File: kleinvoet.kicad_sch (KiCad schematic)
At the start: 33 parts, among them SW101 RESET, SW102 USER, U101 STM32F446RETx, Y101 12 MHz, Y102 32.768 kHz

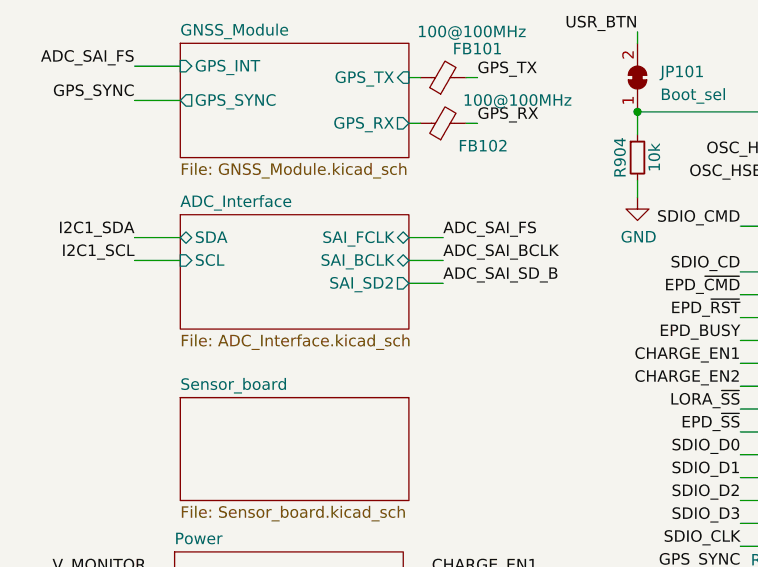
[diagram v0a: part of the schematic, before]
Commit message: (sch) fix SAI pinout
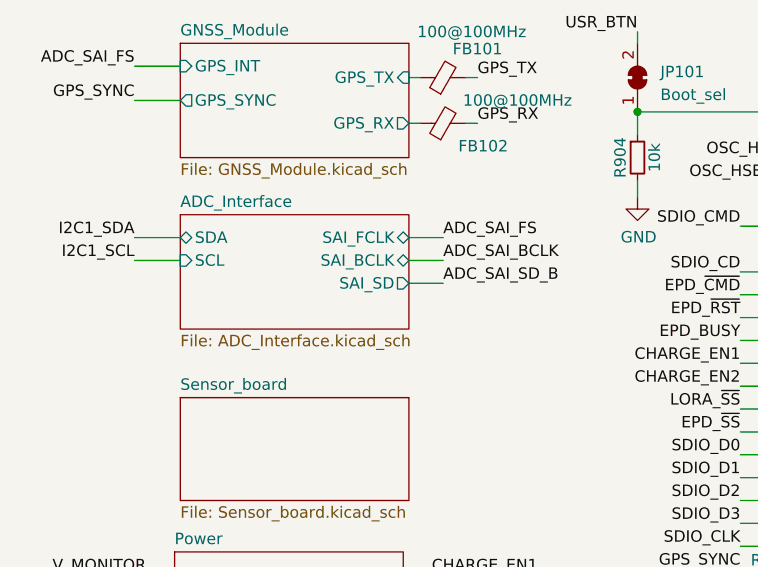
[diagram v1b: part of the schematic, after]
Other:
- sheet ADC_Interface ports: added SAI_SD; removed SAI_SD2
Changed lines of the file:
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@@
       (effects (font (size 1.27 1.27)) (justify left top))
     )
-    (pin "SAI_SD2" output (at 57.15 60.96 0)
+    (pin "SAI_SD" output (at 57.15 60.96 0)
       (effects (font (size 1.27 1.27)) (justify right))
     )

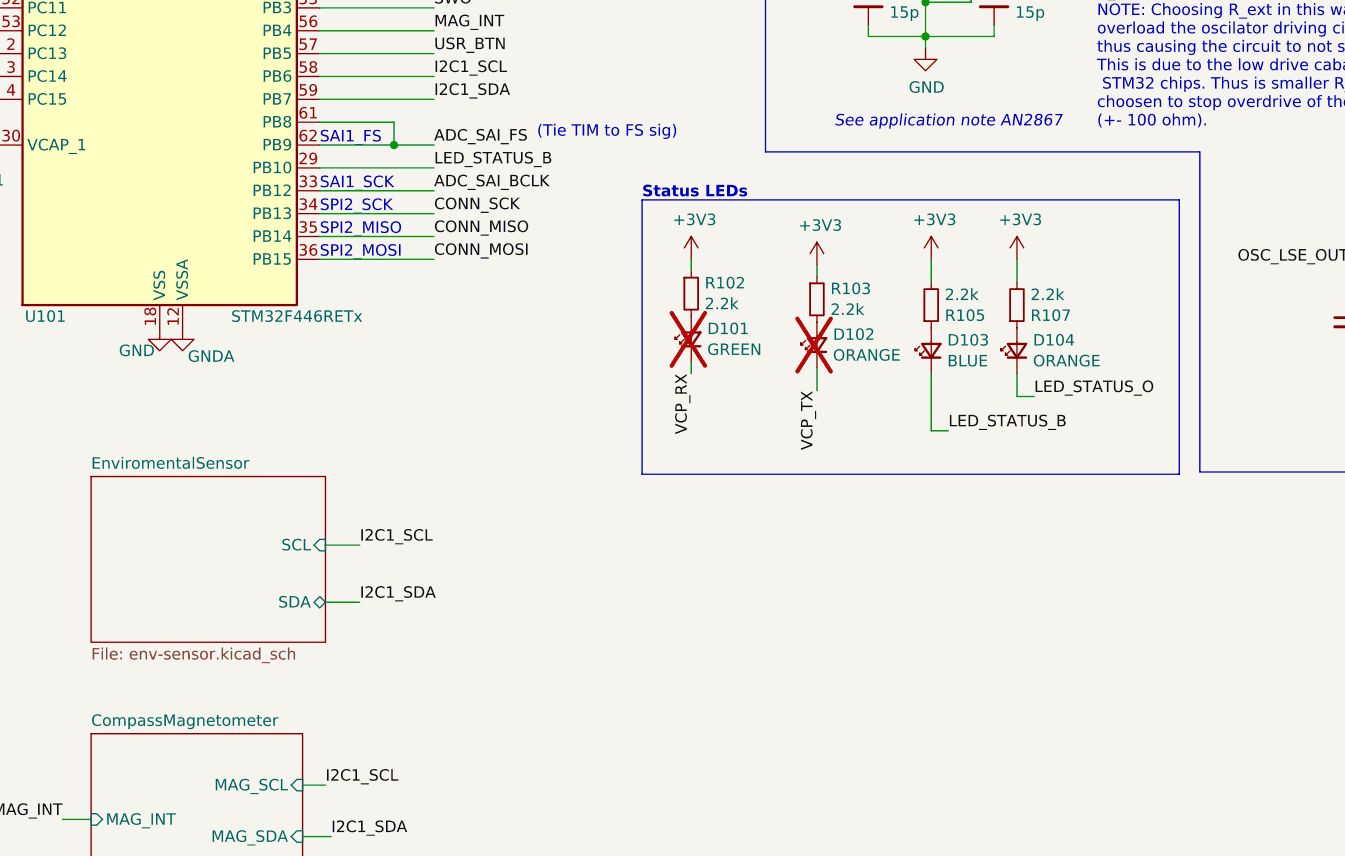
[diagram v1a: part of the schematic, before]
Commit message: (sch) add neopixel placeholder
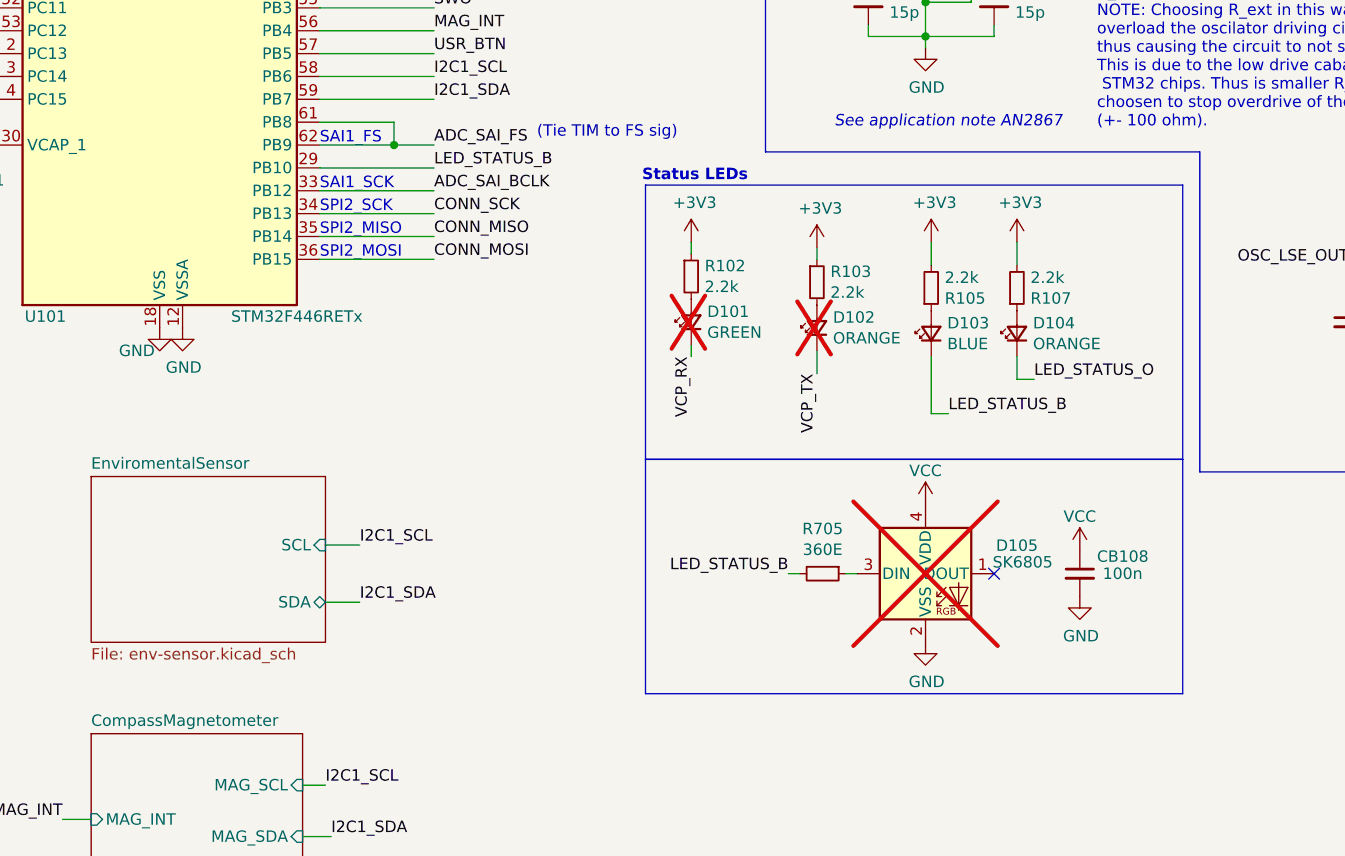
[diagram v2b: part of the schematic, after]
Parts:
- added CB108: 100n, Capacitor_SMD:C_0402_1005Metric, symbol Device:C_Small
- added D105: SK6805, grootvoet:LED_SK6805_PLCC4_2.4x2.7mm_P1.3mm, symbol LED:SK6805
- added R705: 360E, Resistor_SMD:R_0402_1005Metric, symbol Device:R_Small
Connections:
- net GNDA is gone; now on net GND: U101.12 (VSSA)
- net GND: now also CB108.2, D105.2 (VSS)
- net LED_STATUS_B: now also R705.2
- new net: D105.3 (DIN), R705.1
- new net VCC: CB108.1, D105.4 (VDD)
- no-connect marks 0 -> 1
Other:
- moved on the sheet: D101, D102, D103, D104, R102, R103, R105, R107

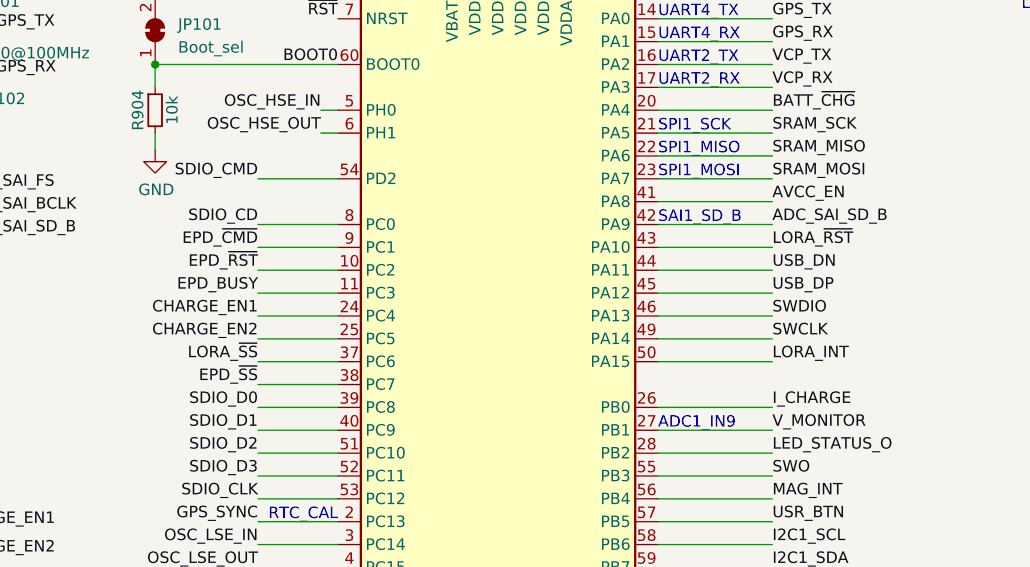
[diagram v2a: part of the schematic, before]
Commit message: (sch) swap LORA_INT & SD_CD pins
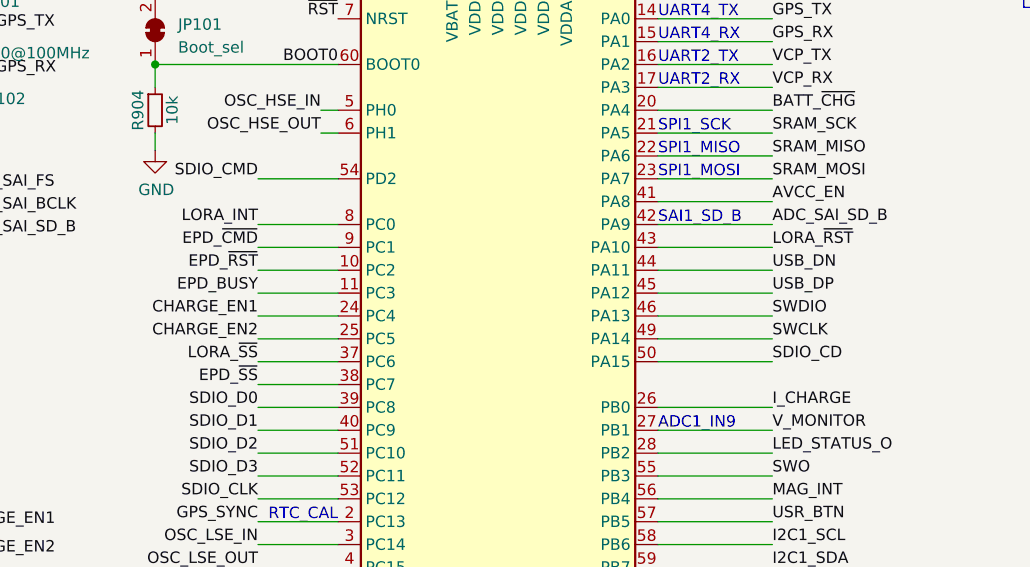
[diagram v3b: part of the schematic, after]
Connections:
- net LORA_INT: now also U101.8 (PC0); no longer U101.50 (PA15)
- net SDIO_CD: now also U101.50 (PA15); no longer U101.8 (PC0)
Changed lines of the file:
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@@
     (effects (font (size 1.27 1.27)) (justify right bottom))
   )
-  (label "SDIO_CD" (at 93.98 59.69 180) (fields_autoplaced)
-    (effects (font (size 1.27 1.27)) (justify right bottom))
+  (label "SDIO_CD" (at 151.13 74.93 0) (fields_autoplaced)
+    (effects (font (size 1.27 1.27)) (justify left bottom))
   )
   (label "VCP_RX" (at 179.705 126.365 270) (fields_autoplaced)
@@
     (effects (font (size 1.27 1.27)) (justify right bottom))
   )
-  (label "LORA_INT" (at 151.13 74.93 0) (fields_autoplaced)
-    (effects (font (size 1.27 1.27)) (justify left bottom))
+  (label "LORA_INT" (at 93.98 59.69 180) (fields_autoplaced)
+    (effects (font (size 1.27 1.27)) (justify right bottom))
   )
   (label "SDIO_D2" (at 30.48 121.92 180) (fields_autoplaced)

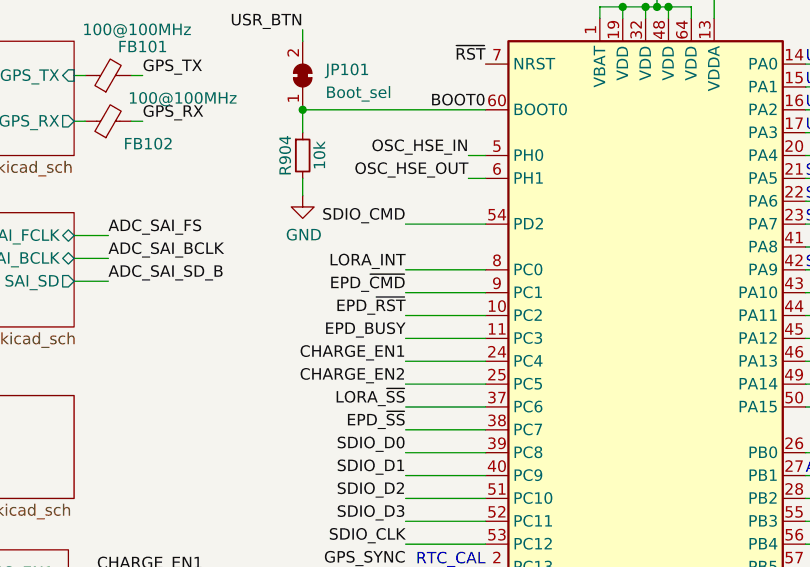
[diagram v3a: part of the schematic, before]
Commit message: (pcb) improve connector routing
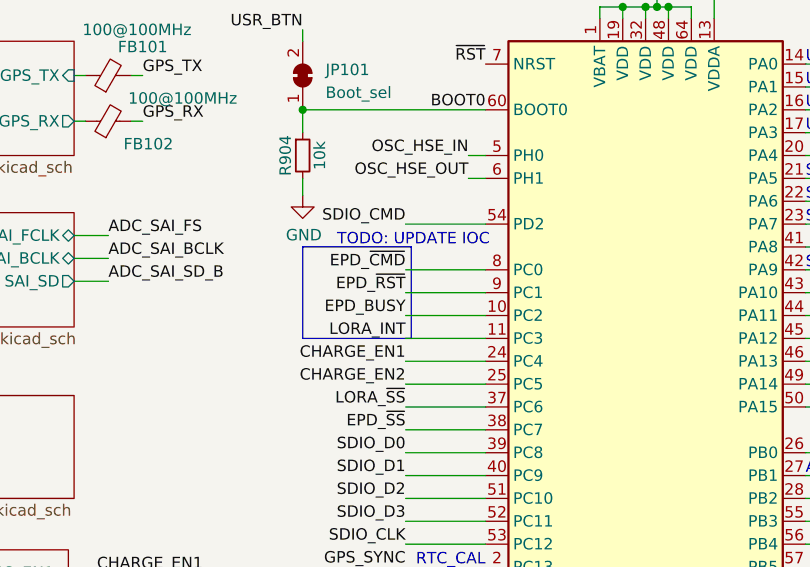
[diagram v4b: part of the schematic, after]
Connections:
- net EPD_BUSY: now also U101.10 (PC2); no longer U101.11 (PC3)
- net EPD_~{CMD}: now also U101.8 (PC0); no longer U101.9 (PC1)
- net EPD_~{RST}: now also U101.9 (PC1); no longer U101.10 (PC2)
- net LORA_INT: now also U101.11 (PC3); no longer U101.8 (PC0)
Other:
- note added: "TODO: UPDATE IOC"
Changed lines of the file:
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@@
+    (fill (type none))
+  )
+  (rectangle (start 82.55 57.15) (end 94.615 67.31)
+    (stroke (width 0) (type default))
     (fill (type none))
   )
@@
     (effects (font (size 1.27 1.27) (thickness 0.254) bold) (justify left bottom))
   )
+  (text "TODO: UPDATE IOC" (at 86.36 57.15 0)
+    (effects (font (size 1.27 1.27)) (justify left bottom))
+  )
   (text "ADC1_IN9" (at 138.43 82.55 0)
     (effects (font (size 1.27 1.27)) (justify left bottom))
@@
     (effects (font (size 1.27 1.27)) (justify left bottom))
   )
-  (label "EPD_BUSY" (at 93.98 67.31 180) (fields_autoplaced)
+  (label "EPD_BUSY" (at 93.98 64.77 180) (fields_autoplaced)
     (effects (font (size 1.27 1.27)) (justify right bottom))
   )
@@
     (effects (font (size 1.27 1.27)) (justify left bottom))
   )
-  (label "EPD_~{CMD}" (at 93.98 62.23 180) (fields_autoplaced)
+  (label "EPD_~{CMD}" (at 93.98 59.69 180) (fields_autoplaced)
     (effects (font (size 1.27 1.27)) (justify right bottom))
   )
@@
     (effects (font (size 1.27 1.27)) (justify left bottom))
   )
-  (label "EPD_~{RST}" (at 93.98 64.77 180) (fields_autoplaced)
+  (label "EPD_~{RST}" (at 93.98 62.23 180) (fields_autoplaced)
     (effects (font (size 1.27 1.27)) (justify right bottom))
   )
@@
     (effects (font (size 1.27 1.27)) (justify right bottom))
   )
-  (label "LORA_INT" (at 93.98 59.69 180) (fields_autoplaced)
-    (effects (font (size 1.27 1.27)) (justify right bottom))
-  )
+  (label "LORA_INT" (at 93.98 67.31 180) (fields_autoplaced)
+    (effects (font (size 1.27 1.27)) (justify right bottom))
+  )

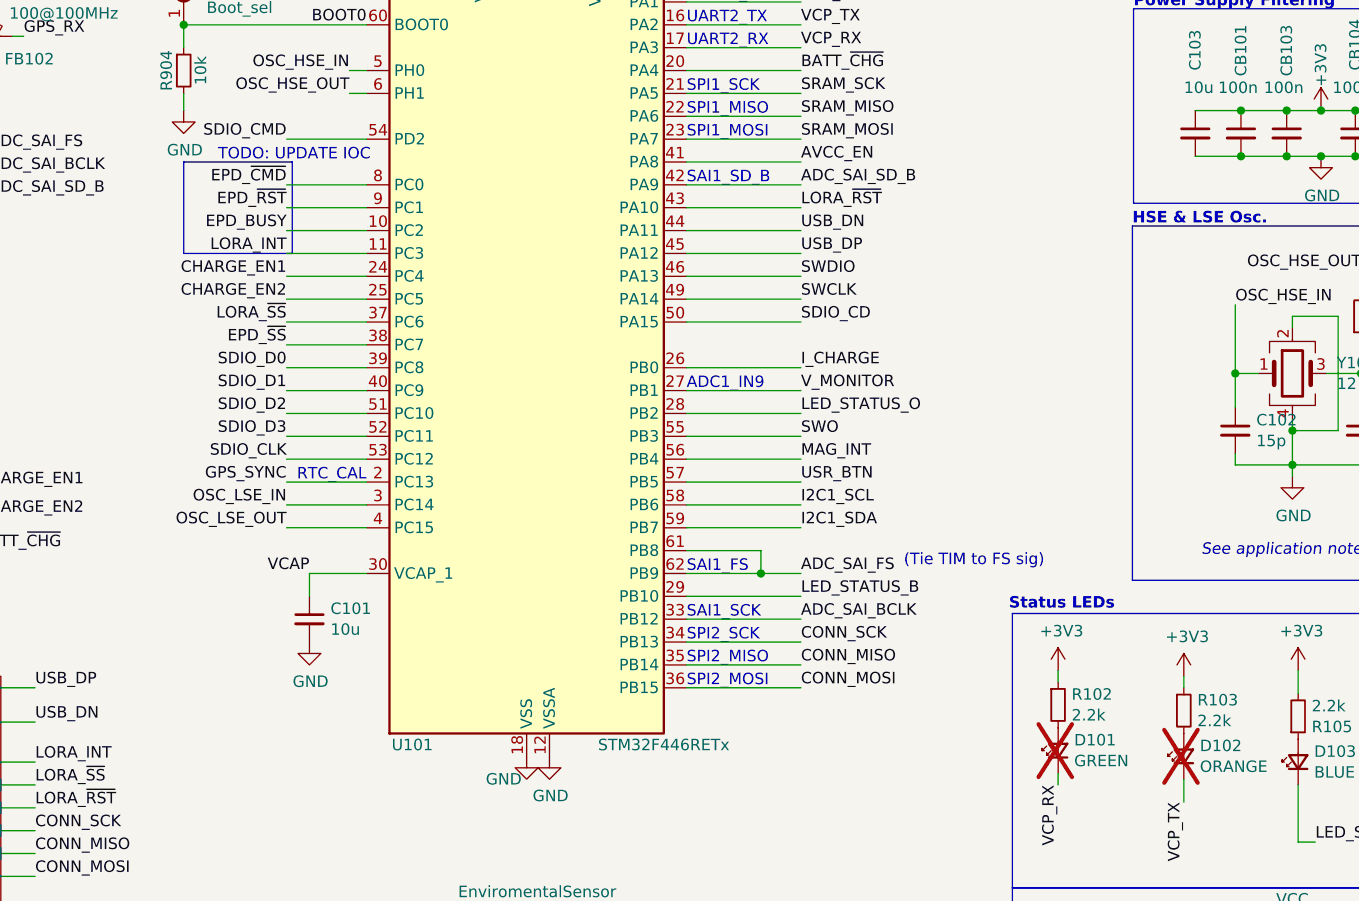
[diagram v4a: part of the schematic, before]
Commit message: (pcb) route power control sec
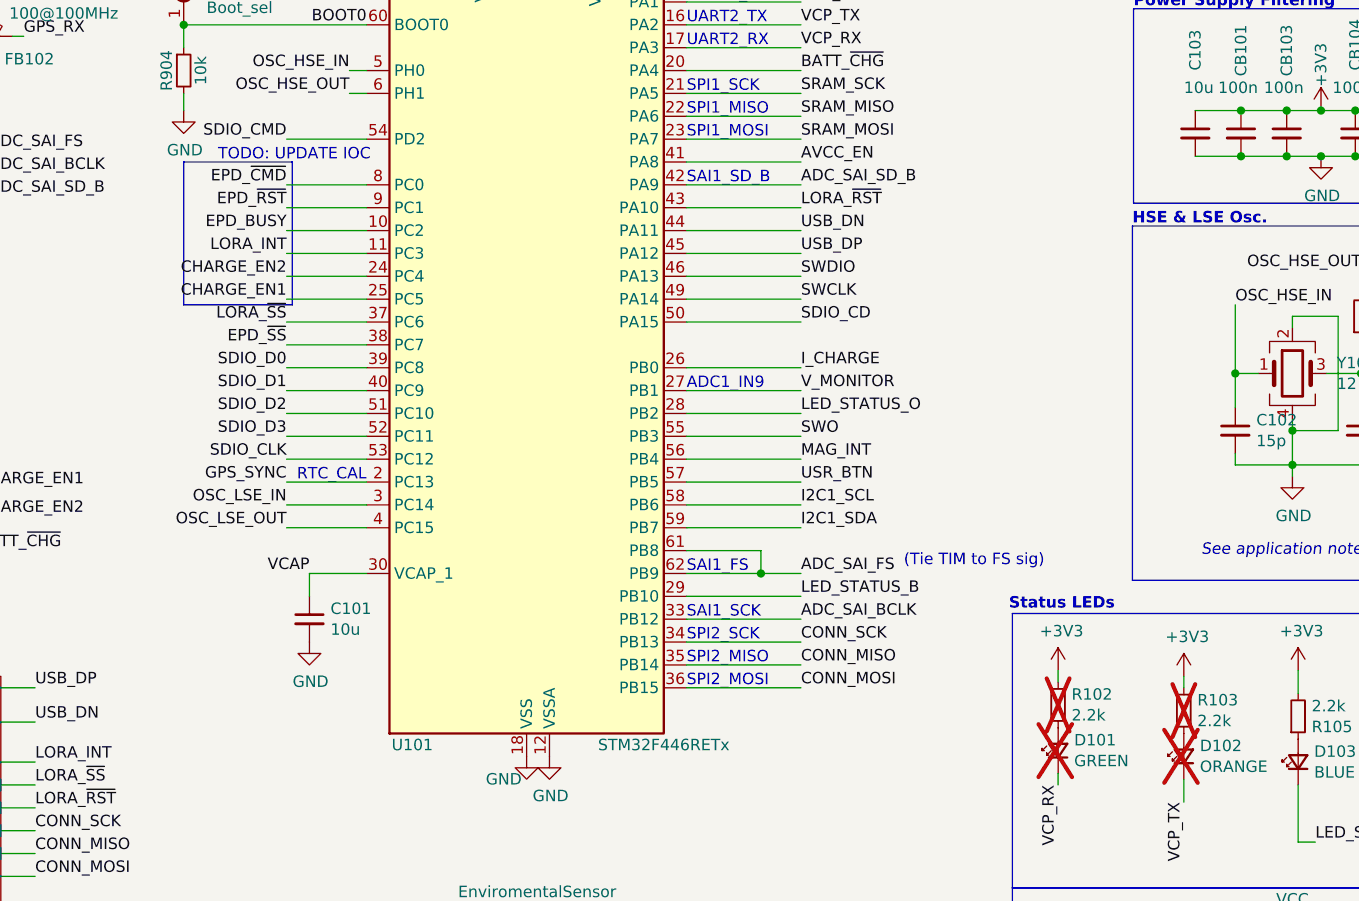
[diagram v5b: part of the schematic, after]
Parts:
- R102, R103: now not fitted
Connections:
- net CHARGE_EN1: now also U101.25 (PC5); no longer U101.24 (PC4)
- net CHARGE_EN2: now also U101.24 (PC4); no longer U101.25 (PC5)
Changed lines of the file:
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@@
     (fill (type none))
   )
-  (rectangle (start 82.55 57.15) (end 94.615 67.31)
+  (rectangle (start 82.55 57.15) (end 94.615 73.025)
     (stroke (width 0) (type default))
     (fill (type none))
@@
     (effects (font (size 1.27 1.27)) (justify right bottom))
   )
-  (label "CHARGE_EN1" (at 93.98 69.85 180) (fields_autoplaced)
+  (label "CHARGE_EN1" (at 93.98 72.39 180) (fields_autoplaced)
     (effects (font (size 1.27 1.27)) (justify right bottom))
   )
@@
     (effects (font (size 1.27 1.27)) (justify right bottom))
   )
-  (label "CHARGE_EN2" (at 93.98 72.39 180) (fields_autoplaced)
+  (label "CHARGE_EN2" (at 93.98 69.85 180) (fields_autoplaced)
     (effects (font (size 1.27 1.27)) (justify right bottom))
   )
@@
   )
   (symbol (lib_id "Device:R_Small") (at 179.705 117.475 0) (unit 1)
-    (in_bom yes) (on_board yes) (dnp no)
+    (in_bom yes) (on_board yes) (dnp yes)
     (property "Reference" "R102" (at 181.2036 116.3066 0)
       (effects (font (size 1.27 1.27)) (justify left))
@@
   )
   (symbol (lib_id "Device:R_Small") (at 193.675 118.11 0) (unit 1)
-    (in_bom yes) (on_board yes) (dnp no)
+    (in_bom yes) (on_board yes) (dnp yes)
     (property "Reference" "R103" (at 195.1736 116.9416 0)
       (effects (font (size 1.27 1.27)) (justify left))
